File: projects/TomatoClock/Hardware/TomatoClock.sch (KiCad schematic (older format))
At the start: 14 parts, among them J1 ICSP, J2 UART, J3 Screen, J4 Ultrasonic, J5 CC2541_Bluetooth, Q1 9014, U1 ATmega328P-PU, Y1 16MHz

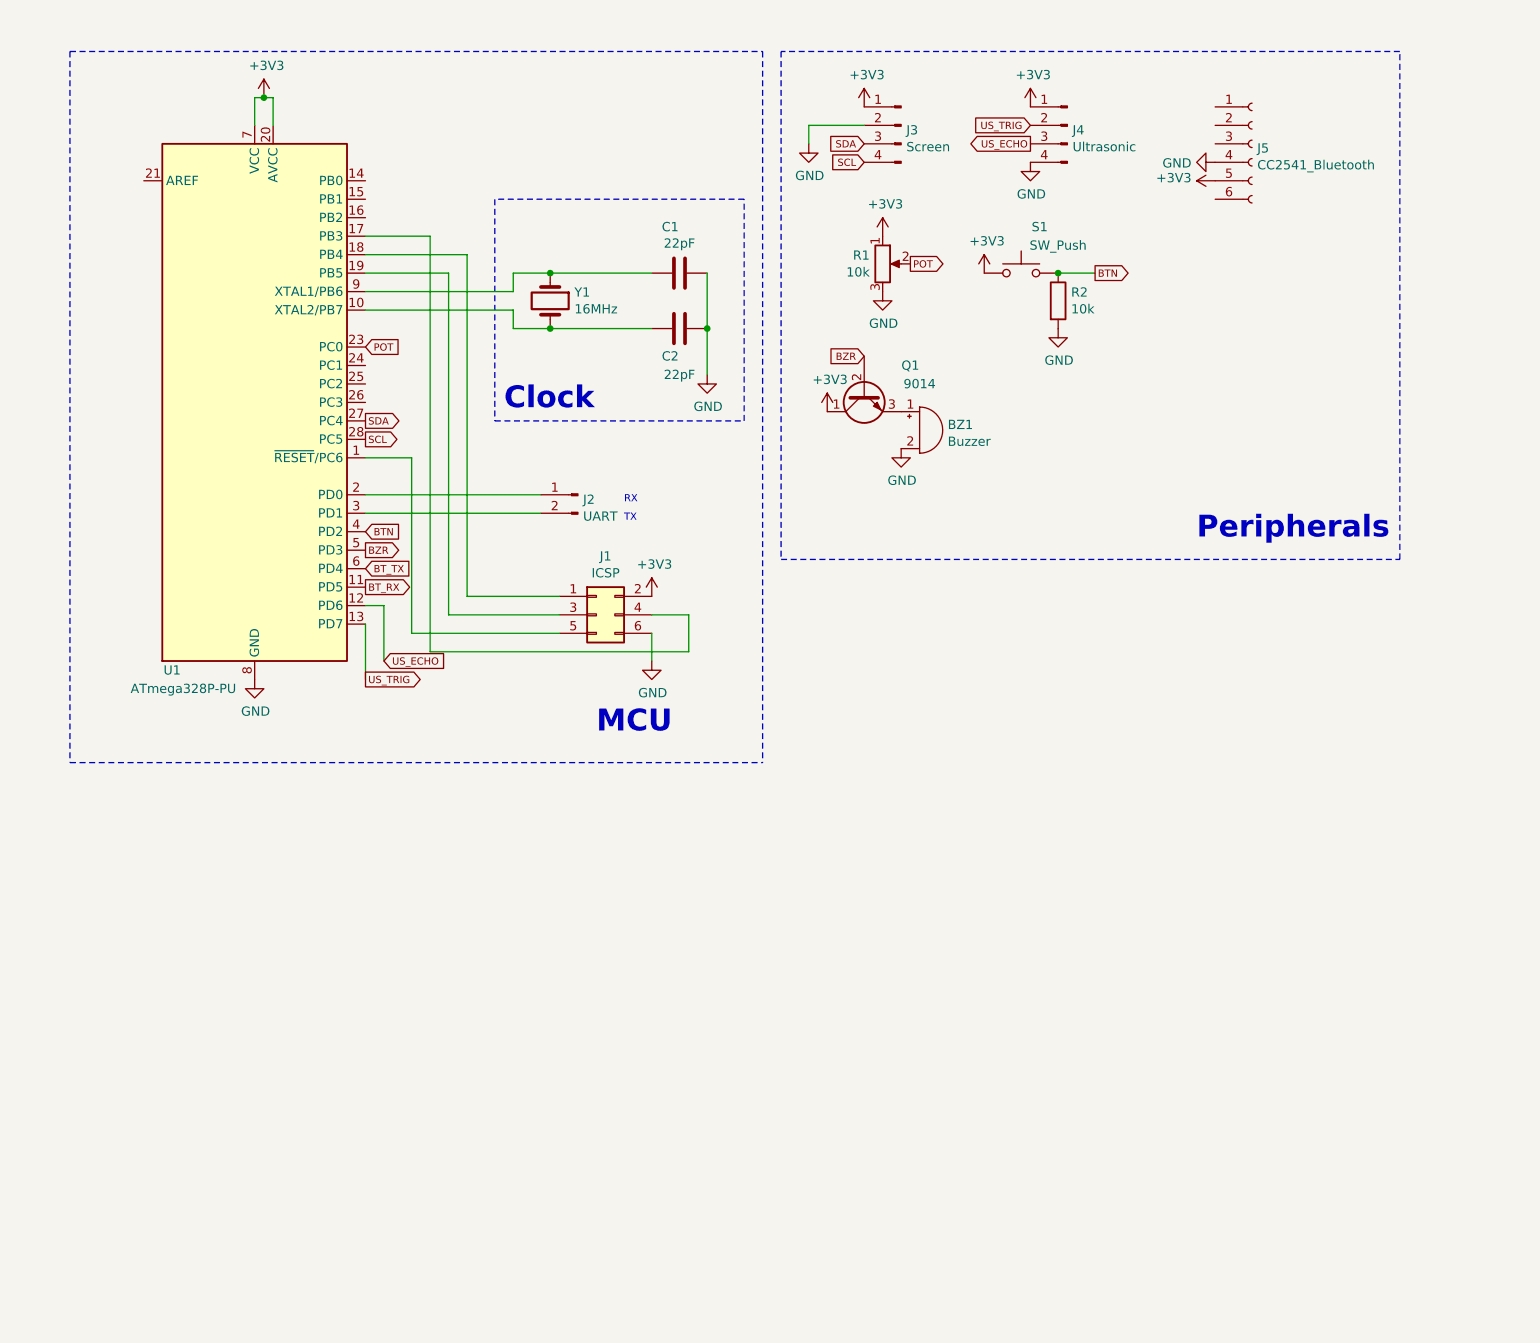
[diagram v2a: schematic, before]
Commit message: TomatoClock: Update Hardware
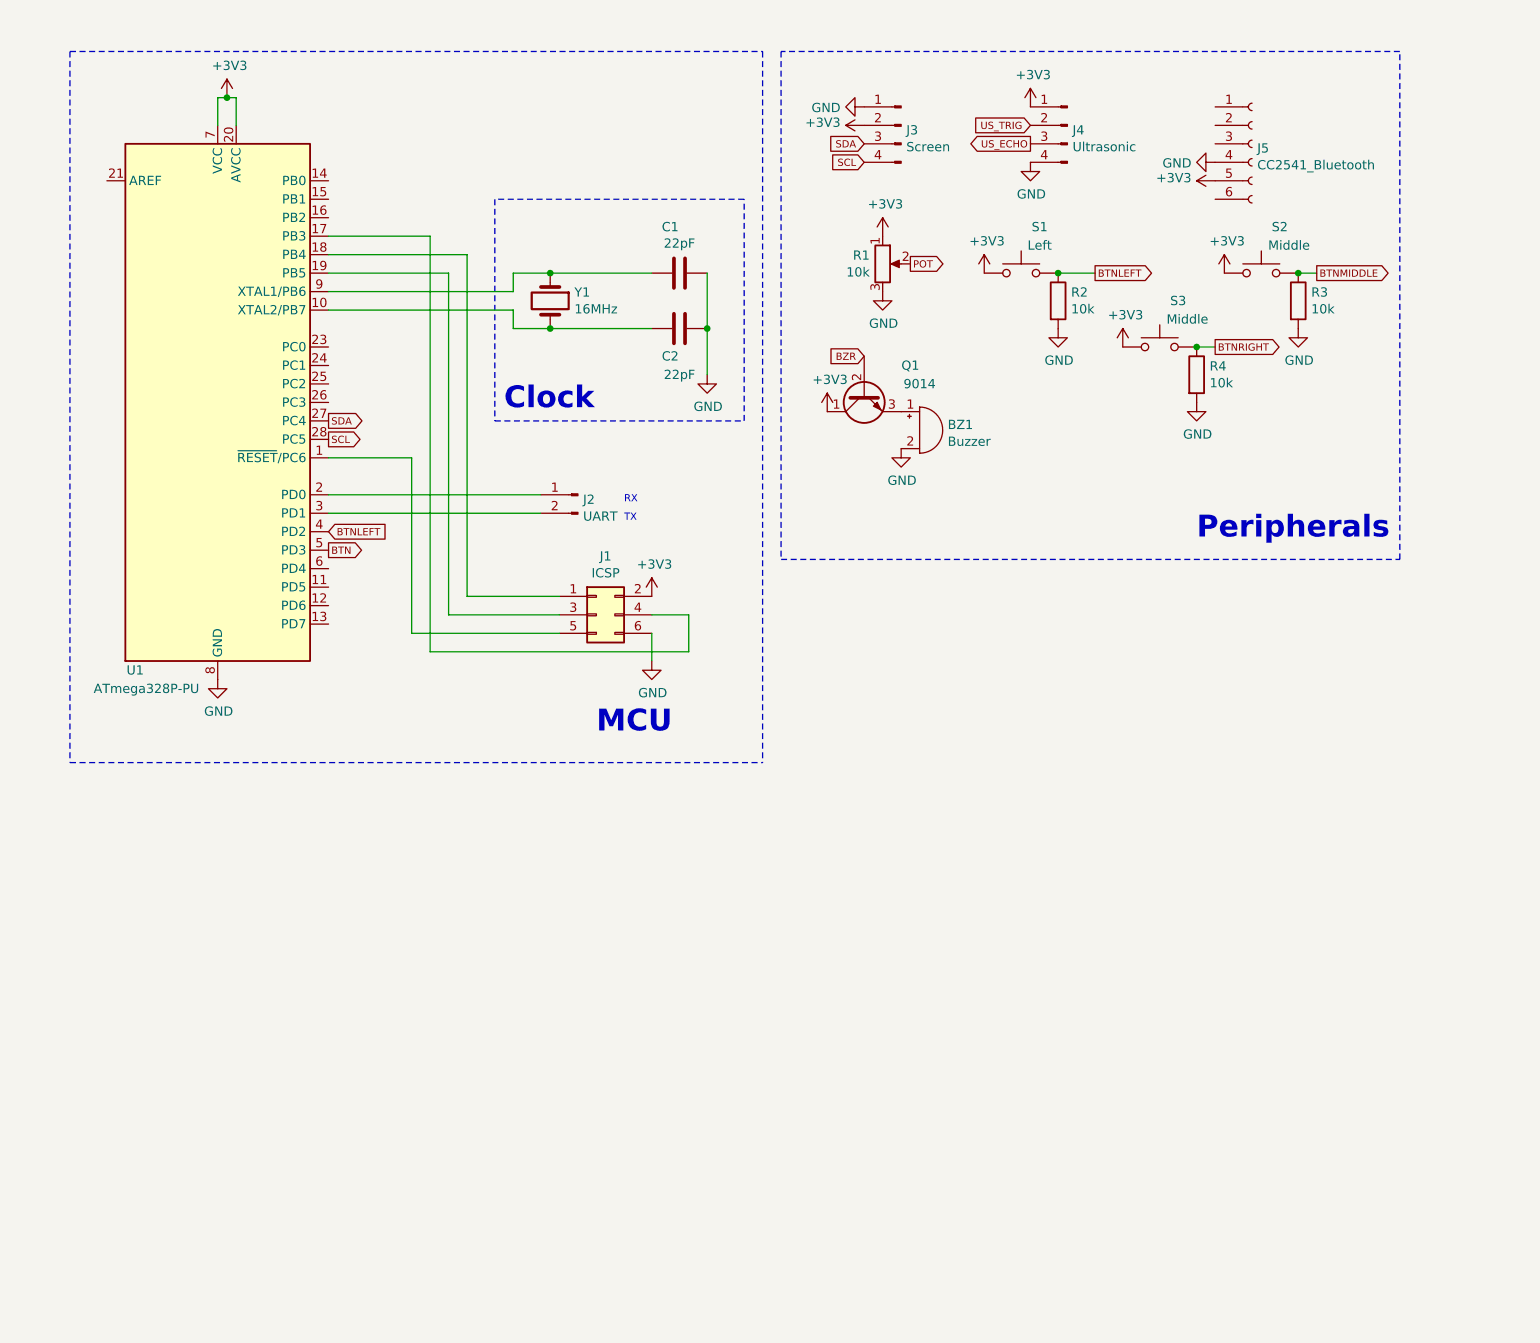
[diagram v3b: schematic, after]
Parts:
- added R3, R4: 10k, symbol Device:R
- added S2, S3: Middle, symbol Switch:SW_Push
- S1: value SW_Push -> Left; footprint (none) -> Button_Switch_THT:SW_PUSH_6mm_H4.3mm
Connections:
- net +3V3: now also J3.2 (Pin_2), S2.1, S3.1; no longer J3.1 (Pin_1)
- net BTN: now also U1.5 (PD3); no longer R2.1, S1.2, U1.4 (PD2)
- net BZR: no longer U1.5 (PD3)
- net GND: now also J3.1 (Pin_1), R3.2, R4.2; no longer J3.2 (Pin_2)
- net POT: no longer U1.23 (PC0)
- net US_ECHO: no longer U1.12 (PD6)
- net US_TRIG: no longer U1.13 (PD7)
- net BT_RX: no longer names the net of U1.11 (PD5)
- net BT_TX: no longer names the net of U1.6 (PD4)
- new net BTNLEFT: R2.1, S1.2, U1.4 (PD2)
- new net BTNMIDDLE: R3.1, S2.2
- new net BTNRIGHT: R4.1, S3.2
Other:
- moved on the sheet: U1
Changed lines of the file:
@@
 L power:+3V3 #PWR0101
 U 1 1 6190BA27
-P 1850 1000
-F 0 "#PWR0101" H 1850 850 50  0001 C CNN
-F 1 "+3V3" H 1865 1173 50  0000 C CNN
-F 2 "" H 1850 1000 50  0001 C CNN
-F 3 "" H 1850 1000 50  0001 C CNN
-	1    1850 1000
-	1    0    0    -1
-$EndComp
-Wire Wire Line
-	1850 1000 1800 1000
-Wire Wire Line
-	1800 1000 1800 1150
-Wire Wire Line
-	1850 1000 1900 1000
-Wire Wire Line
-	1900 1000 1900 1150
-Connection ~ 1850 1000
+P 1650 1000
+F 0 "#PWR0101" H 1650 850 50  0001 C CNN
+F 1 "+3V3" H 1665 1173 50  0000 C CNN
+F 2 "" H 1650 1000 50  0001 C CNN
+F 3 "" H 1650 1000 50  0001 C CNN
+	1    1650 1000
+	1    0    0    -1
+$EndComp
+Wire Wire Line
+	1650 1000 1600 1000
+Wire Wire Line
+	1600 1000 1600 1150
+Wire Wire Line
+	1650 1000 1700 1000
+Wire Wire Line
+	1700 1000 1700 1150
+Connection ~ 1650 1000
 $Comp
 L Device:Crystal Y1
@@
 L power:GND #PWR0103
 U 1 1 6191656C
-P 1800 4150
-F 0 "#PWR0103" H 1800 3900 50  0001 C CNN
-F 1 "GND" H 1805 3977 50  0000 C CNN
-F 2 "" H 1800 4150 50  0001 C CNN
-F 3 "" H 1800 4150 50  0001 C CNN
-	1    1800 4150
+P 1600 4150
+F 0 "#PWR0103" H 1600 3900 50  0001 C CNN
+F 1 "GND" H 1605 3977 50  0000 C CNN
+F 2 "" H 1600 4150 50  0001 C CNN
+F 3 "" H 1600 4150 50  0001 C CNN
+	1    1600 4150
 	1    0    0    -1
 $EndComp
@@
 	-1   0    0    -1
 $EndComp
-$Comp
-L power:+3V3 #PWR0104
-U 1 1 6192D813
-P 5100 1050
-F 0 "#PWR0104" H 5100 900 50  0001 C CNN
-F 1 "+3V3" H 5115 1223 50  0000 C CNN
-F 2 "" H 5100 1050 50  0001 C CNN
-F 3 "" H 5100 1050 50  0001 C CNN
-	1    5100 1050
-	1    0    0    -1
-$EndComp
-$Comp
-L power:GND #PWR0105
-U 1 1 6192DD9D
-P 4800 1250
-F 0 "#PWR0105" H 4800 1000 50  0001 C CNN
-F 1 "GND" H 4805 1077 50  0000 C CNN
-F 2 "" H 4800 1250 50  0001 C CNN
-F 3 "" H 4800 1250 50  0001 C CNN
-	1    4800 1250
-	1    0    0    -1
-$EndComp
 Text GLabel 5100 1250 0    39   Input ~ 0
 SDA
@@
 Text Notes 3150 2700 0    118  ~ 24
 Clock
-Text GLabel 2400 2750 2    39   Output ~ 0
+Text GLabel 2200 2750 2    39   Output ~ 0
 SDA
-Text GLabel 2400 2850 2    39   Output ~ 0
+Text GLabel 2200 2850 2    39   Output ~ 0
 SCL
 Wire Notes Line
@@
 $EndComp
 Wire Wire Line
-	2400 2150 3200 2150
-Wire Wire Line
-	2400 1850 2950 1850
-Wire Wire Line
 	2950 1850 2950 3700
 Wire Wire Line
 	2950 3700 3450 3700
 Wire Wire Line
-	2400 1950 2850 1950
-Wire Wire Line
 	2850 1950 2850 3800
 Wire Wire Line
 	2850 3800 3450 3800
 Wire Wire Line
-	2400 1750 2750 1750
-Wire Wire Line
 	2750 4000 4150 4000
 Wire Wire Line
@@
 Wire Wire Line
 	4150 3800 3950 3800
-Wire Wire Line
-	2400 2950 2650 2950
 Wire Wire Line
 	2650 2950 2650 3900
@@
 	1    0    0    -1
 $EndComp
-Wire Wire Line
-	5100 1150 4800 1150
-Wire Wire Line
-	4800 1150 4800 1250
 $Comp
 L power:GND #PWR0109
@@
 	1    0    0    -1
 $EndComp
-Text GLabel 2400 2350 2    39   Input ~ 0
-POT
 Text GLabel 5350 1900 2    39   Output ~ 0
 POT
@@
 P 5950 1950
 F 0 "S1" H 6050 2200 50  0000 C CNN
-F 1 "SW_Push" H 6150 2100 50  0000 C CNN
-F 2 "" H 5950 2150 50  0001 C CNN
+F 1 "Left" H 6050 2100 50  0000 C CNN
+F 2 "Button_Switch_THT:SW_PUSH_6mm_H4.3mm" H 5950 2150 50  0001 C CNN
 F 3 "~" H 5950 2150 50  0001 C CNN
 	1    5950 1950
@@
 	1    0    0    -1
 $EndComp
-Text GLabel 2400 4150 2    39   Output ~ 0
-US_TRIG
-Text GLabel 2500 4050 2    39   Input ~ 0
-US_ECHO
-Wire Wire Line
-	2400 3850 2400 4150
-Wire Wire Line
-	2500 4050 2500 3750
-Wire Wire Line
-	2500 3750 2400 3750
-Text GLabel 2400 3350 2    39   Input ~ 0
-BTN
+Text GLabel 2200 3350 2    39   Input ~ 0
+BTNLEFT
 $Comp
 L Connector:Conn_01x02_Male J2
@@
 	-1   0    0    -1
 $EndComp
-Wire Wire Line
-	2400 3150 3350 3150
 Text Notes 3800 3200 0    39   ~ 0
 RX
@@
 TX
 Text GLabel 6350 1950 2    39   Output ~ 0
-BTN
+BTNLEFT
 Wire Wire Line
 	6150 1950 6350 1950
@@
 Text GLabel 5100 2400 0    39   Input ~ 0
 BZR
-Text GLabel 2400 3450 2    39   Output ~ 0
-BZR
 $Comp
 L Connector:Conn_01x06_Female J5
@@
 	0    1    1    0
 $EndComp
-Text GLabel 2400 3550 2    39   Input ~ 0
-BT_TX
-Wire Wire Line
-	2400 2050 3200 2050
-Wire Wire Line
-	3350 3250 2400 3250
 $Comp
 L MCU_Microchip_ATmega:ATmega328P-PU U1
 U 1 1 619084B6
-P 1800 2650
-F 0 "U1" H 1400 1200 50  0000 R CNN
-F 1 "ATmega328P-PU" H 1700 1100 50  0000 R CNN
-F 2 "Package_DIP:DIP-28_W7.62mm" H 1800 2650 50  0001 C CIN
-F 3 "http://ww1.microchip.com/downloads/en/DeviceDoc/ATmega328_P%20AVR%20MCU%20with%20picoPower%20Technology%20Data%20Sheet%2040001984A.pdf" H 1800 2650 50  0001 C CNN
-	1    1800 2650
-	1    0    0    -1
-$EndComp
-Text GLabel 2400 3650 2    39   Output ~ 0
-BT_RX
+P 1600 2650
+F 0 "U1" H 1200 1200 50  0000 R CNN
+F 1 "ATmega328P-PU" H 1500 1100 50  0000 R CNN
+F 2 "Package_DIP:DIP-28_W7.62mm" H 1600 2650 50  0001 C CIN
+F 3 "http://ww1.microchip.com/downloads/en/DeviceDoc/ATmega328_P%20AVR%20MCU%20with%20picoPower%20Technology%20Data%20Sheet%2040001984A.pdf" H 1600 2650 50  0001 C CNN
+	1    1600 2650
+	1    0    0    -1
+$EndComp
+$Comp
+L power:GND #PWR?
+U 1 1 619D469C
+P 5100 1050
+F 0 "#PWR?" H 5100 800 50  0001 C CNN
+F 1 "GND" V 5105 922 50  0000 R CNN
+F 2 "" H 5100 1050 50  0001 C CNN
+F 3 "" H 5100 1050 50  0001 C CNN
+	1    5100 1050
+	0    1    1    0
+$EndComp
+$Comp
+L power:+3V3 #PWR?
+U 1 1 619D4D4D
+P 5100 1150
+F 0 "#PWR?" H 5100 1000 50  0001 C CNN
+F 1 "+3V3" V 5115 1278 50  0000 L CNN
+F 2 "" H 5100 1150 50  0001 C CNN
+F 3 "" H 5100 1150 50  0001 C CNN
+	1    5100 1150
+	0    -1   -1   0
+$EndComp
+Wire Wire Line
+	2200 1750 2750 1750
+Wire Wire Line
+	2200 1850 2950 1850
+Wire Wire Line
+	2200 1950 2850 1950
+Wire Wire Line
+	2200 2050 3200 2050
+Wire Wire Line
+	2200 2150 3200 2150
+Wire Wire Line
+	2200 2950 2650 2950
+Wire Wire Line
+	2200 3150 3350 3150
+Wire Wire Line
+	2200 3250 3350 3250
+$Comp
+L Switch:SW_Push S2
+U 1 1 619F84CA
+P 7250 1950
+F 0 "S2" H 7350 2200 50  0000 C CNN
+F 1 "Middle" H 7400 2100 50  0000 C CNN
+F 2 "" H 7250 2150 50  0001 C CNN
+F 3 "~" H 7250 2150 50  0001 C CNN
+	1    7250 1950
+	1    0    0    -1
+$EndComp
+$Comp
+L power:+3V3 #PWR?
+U 1 1 619FB7CA
+P 7050 1950
+F 0 "#PWR?" H 7050 1800 50  0001 C CNN
+F 1 "+3V3" H 7065 2123 50  0000 C CNN
+F 2 "" H 7050 1950 50  0001 C CNN
+F 3 "" H 7050 1950 50  0001 C CNN
+	1    7050 1950
+	1    0    0    -1
+$EndComp
+$Comp
+L Device:R R3
+U 1 1 619FC2AA
+P 7450 2100
+F 0 "R3" H 7520 2146 50  0000 L CNN
+F 1 "10k" H 7520 2055 50  0000 L CNN
+F 2 "" V 7380 2100 50  0001 C CNN
+F 3 "~" H 7450 2100 50  0001 C CNN
+	1    7450 2100
+	1    0    0    -1
+$EndComp
+$Comp
+L power:GND #PWR?
+U 1 1 619FCCC1
+P 7450 2250
+F 0 "#PWR?" H 7450 2000 50  0001 C CNN
+F 1 "GND" H 7455 2077 50  0000 C CNN
+F 2 "" H 7450 2250 50  0001 C CNN
+F 3 "" H 7450 2250 50  0001 C CNN
+	1    7450 2250
+	1    0    0    -1
+$EndComp
+Text GLabel 7550 1950 2    39   Output ~ 0
+BTNMIDDLE
+Wire Wire Line
+	7550 1950 7450 1950
+Connection ~ 7450 1950
+$Comp
+L Switch:SW_Push S3
+U 1 1 61A04CF4
+P 6700 2350
+F 0 "S3" H 6800 2600 50  0000 C CNN
+F 1 "Middle" H 6850 2500 50  0000 C CNN
+F 2 "" H 6700 2550 50  0001 C CNN
+F 3 "~" H 6700 2550 50  0001 C CNN
+	1    6700 2350
+	1    0    0    -1
+$EndComp
+$Comp
+L power:+3V3 #PWR?
+U 1 1 61A04CFA
+P 6500 2350
+F 0 "#PWR?" H 6500 2200 50  0001 C CNN
+F 1 "+3V3" H 6515 2523 50  0000 C CNN
+F 2 "" H 6500 2350 50  0001 C CNN
+F 3 "" H 6500 2350 50  0001 C CNN
+	1    6500 2350
+	1    0    0    -1
+$EndComp
+$Comp
+L Device:R R4
+U 1 1 61A04D00
+P 6900 2500
+F 0 "R4" H 6970 2546 50  0000 L CNN
+F 1 "10k" H 6970 2455 50  0000 L CNN
+F 2 "" V 6830 2500 50  0001 C CNN
+F 3 "~" H 6900 2500 50  0001 C CNN
+	1    6900 2500
+	1    0    0    -1
+$EndComp
+$Comp
+L power:GND #PWR?
+U 1 1 61A04D06
+P 6900 2650
+F 0 "#PWR?" H 6900 2400 50  0001 C CNN
+F 1 "GND" H 6905 2477 50  0000 C CNN
+F 2 "" H 6900 2650 50  0001 C CNN
+F 3 "" H 6900 2650 50  0001 C CNN
+	1    6900 2650
+	1    0    0    -1
+$EndComp
+Text GLabel 7000 2350 2    39   Output ~ 0
+BTNRIGHT
+Wire Wire Line
+	7000 2350 6900 2350
+Connection ~ 6900 2350
+Text GLabel 2200 3450 2    39   Output ~ 0
+BTN
 $EndSCHEMATC

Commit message: TomatoClock: Update PCB footprints and schematics
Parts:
- S2, S3: footprint (none) -> Button_Switch_THT:SW_PUSH_6mm_H4.3mm
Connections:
- net BZR is gone; now on net BUZZER: Q1.2 (B)
- net BTNRIGHT: now also U1.6 (PD4)
- net US_ECHO: now also U1.12 (PD6)
- net US_TRIG: now also U1.11 (PD5)
- net BT_TX: now reaches U1.13 (PD7)
- net BT_TX: now also J5.3 (Pin_3)
- net BT_RX: now reaches U1.14 (PB0)
- net BT_RX: now also J5.2 (Pin_2)
- net PWM_SIGNAL: now reaches U1.15 (PB1)
- net BUZZER: now reaches U1.16 (PB2)
- net BTN renamed BTNENTER
- no-connect marks 0 -> 2
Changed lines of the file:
@@
 $EndComp
 Text GLabel 5100 2400 0    39   Input ~ 0
-BZR
+BUZZER
 $Comp
 L Connector:Conn_01x06_Female J5
@@
 F 0 "S2" H 7350 2200 50  0000 C CNN
 F 1 "Middle" H 7400 2100 50  0000 C CNN
-F 2 "" H 7250 2150 50  0001 C CNN
+F 2 "Button_Switch_THT:SW_PUSH_6mm_H4.3mm" H 7250 2150 50  0001 C CNN
 F 3 "~" H 7250 2150 50  0001 C CNN
 	1    7250 1950
@@
 F 0 "S3" H 6800 2600 50  0000 C CNN
 F 1 "Middle" H 6850 2500 50  0000 C CNN
-F 2 "" H 6700 2550 50  0001 C CNN
+F 2 "Button_Switch_THT:SW_PUSH_6mm_H4.3mm" H 6700 2550 50  0001 C CNN
 F 3 "~" H 6700 2550 50  0001 C CNN
 	1    6700 2350
@@
 	7000 2350 6900 2350
 Connection ~ 6900 2350
-Text GLabel 2200 3450 2    39   Output ~ 0
-BTN
+Text GLabel 2200 3450 2    39   Input ~ 0
+BTNENTER
+Text GLabel 2200 3550 2    39   Input ~ 0
+BTNRIGHT
+Text GLabel 2200 3650 2    39   Output ~ 0
+US_TRIG
+Text GLabel 2200 3750 2    39   Input ~ 0
+US_ECHO
+Text GLabel 2200 3850 2    39   Input ~ 0
+BT_TX
+Text GLabel 2200 1450 2    39   Output ~ 0
+BT_RX
+Text GLabel 2200 1650 2    39   Output ~ 0
+BUZZER
+Text GLabel 2200 1550 2    39   Output ~ 0
+PWM_SIGNAL
+Text GLabel 7000 1150 0    39   Input ~ 0
+BT_RX
+Text GLabel 7000 1250 0    39   Output ~ 0
+BT_TX
+NoConn ~ 7000 1050
+NoConn ~ 7000 1550
 $EndSCHEMATC
